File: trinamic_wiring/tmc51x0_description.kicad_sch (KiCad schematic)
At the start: 2 parts, among them M3 Stepper_Motor_QSH2818-32-07-0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

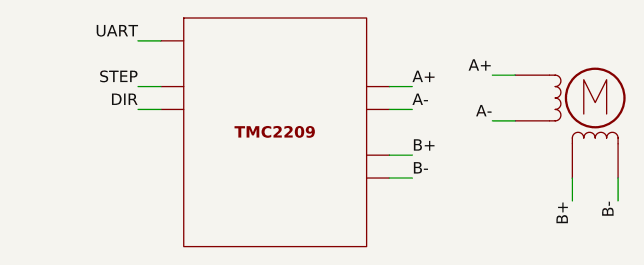
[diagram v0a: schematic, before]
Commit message: Remove unused sheets
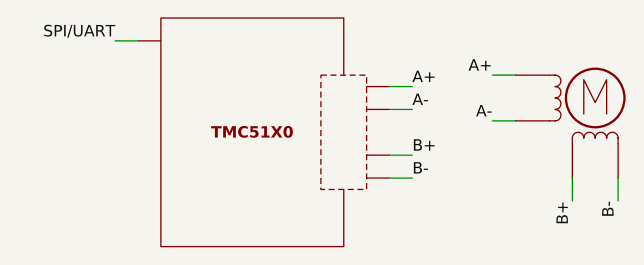
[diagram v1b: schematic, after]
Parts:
- removed TMC13: DOC_TMC2209, symbol Janelia:DOC_TMC2209
- added TMC51X1: TMC51X0_DOC, symbol Janelia:TMC51X0_DOC
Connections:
- net A+: now also TMC51X1.5 (OA1)
- net A-: now also TMC51X1.6 (OA2)
- net B+: now also TMC51X1.7 (OB1)
- net B-: now also TMC51X1.8 (OB2)
- new net SPI/UART: TMC51X1.0 (SPI/UART)
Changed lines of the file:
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@@
   (title_block
     (title "Trinamic Wiring")
-    (date "2023-08-02")
+    (date "2024-01-31")
     (rev "0.4")
     (company "Janelia Research Campus")
@@
     (stroke (width 0) (type default))
   )
-  (wire (pts (xy 119.38 81.28) (xy 121.92 81.28))
+  (wire (pts (xy 116.84 81.28) (xy 119.38 81.28))
     (stroke (width 0) (type default))
   )
@@
     (stroke (width 0) (type default))
   )
-  (wire (pts (xy 119.38 88.9) (xy 121.92 88.9))
-    (stroke (width 0) (type default))
-  )
   (wire (pts (xy 149.86 86.36) (xy 147.32 86.36))
     (stroke (width 0) (type default))
   )
   (wire (pts (xy 172.72 99.06) (xy 172.72 96.52))
-    (stroke (width 0) (type default))
-  )
-  (wire (pts (xy 119.38 86.36) (xy 121.92 86.36))
     (stroke (width 0) (type default))
   )
@@
     (effects (font (size 1.27 1.27)) (justify left bottom))
   )
-  (label "STEP" (at 119.38 86.36 180) (fields_autoplaced)
-    (effects (font (size 1.27 1.27)) (justify right bottom))
-  )
   (label "A+" (at 158.75 85.09 180) (fields_autoplaced)
     (effects (font (size 1.27 1.27)) (justify right bottom))
@@
     (effects (font (size 1.27 1.27)) (justify left bottom))
   )
-  (label "UART" (at 119.38 81.28 180) (fields_autoplaced)
+  (label "SPI{slash}UART" (at 116.84 81.28 180) (fields_autoplaced)
     (effects (font (size 1.27 1.27)) (justify right bottom))
   )
@@
   )
   (label "B-" (at 172.72 99.06 270) (fields_autoplaced)
-    (effects (font (size 1.27 1.27)) (justify right bottom))
-  )
-  (label "DIR" (at 119.38 88.9 180) (fields_autoplaced)
     (effects (font (size 1.27 1.27)) (justify right bottom))
   )
@@
     (instances
       (project "trinamic_wiring"
-        (path "/e4144788-6304-493f-818e-5d881d3b7418/c8eda2b5-ab13-4033-82d9-875c9fcaf884/8277c47e-3fcc-48ef-9892-6d34b4c51a79"
-          (reference "M3") (unit 1)
-        )
         (path "/e4144788-6304-493f-818e-5d881d3b7418/a161638e-a96f-4455-865a-1d7502675f43/8277c47e-3fcc-48ef-9892-6d34b4c51a79"
           (reference "M3") (unit 1)
@@
     )
   )
-  (symbol (lib_id "Janelia:DOC_TMC2209") (at 134.62 91.44 0) (unit 1)
+  (symbol (lib_id "Janelia:TMC51X0_DOC") (at 132.08 91.44 0) (unit 1)
     (in_bom yes) (on_board yes) (dnp no) (fields_autoplaced)
-    (property "Reference" "TMC13" (at 134.62 72.39 0)
+    (property "Reference" "TMC51X1" (at 132.08 72.39 0)
       (effects (font (size 1.27 1.27)) hide)
     )
-    (property "Value" "DOC_TMC2209" (at 134.62 77.47 0)
+    (property "Value" "TMC51X0_DOC" (at 132.08 77.47 0)
       (effects (font (size 1.524 1.524)) hide)
     )
-    (property "Footprint" "" (at 132.08 118.11 0)
+    (property "Footprint" "" (at 129.54 118.11 0)
       (effects (font (size 1.524 1.524)) hide)
     )
-    (property "Datasheet" "" (at 134.62 91.44 0)
+    (property "Datasheet" "" (at 132.08 91.44 0)
       (effects (font (size 1.524 1.524)) hide)
     )
-    (property "Sim.Enable" "0" (at 134.62 74.93 0)
+    (property "Sim.Enable" "0" (at 132.08 74.93 0)
       (effects (font (size 1.27 1.27)) hide)
     )
-    (pin "0")
+    (pin "8")
+    (pin "10")
+    (pin "9")
+    (pin "7")
+    (pin "6")
+    (pin "5")
     (pin "1")
-    (pin "10")
-    (pin "2")
     (pin "3")
     (pin "4")
-    (pin "5")
-    (pin "6")
-    (pin "7")
-    (pin "8")
-    (pin "9")
+    (pin "2")
+    (pin "0")
     (instances
       (project "trinamic_wiring"
-        (path "/e4144788-6304-493f-818e-5d881d3b7418/c8eda2b5-ab13-4033-82d9-875c9fcaf884/8277c47e-3fcc-48ef-9892-6d34b4c51a79"
-          (reference "TMC13") (unit 1)
-        )
         (path "/e4144788-6304-493f-818e-5d881d3b7418/a161638e-a96f-4455-865a-1d7502675f43/8277c47e-3fcc-48ef-9892-6d34b4c51a79"
-          (reference "TMC13") (unit 1)
+          (reference "TMC51X1") (unit 1)
         )
       )
